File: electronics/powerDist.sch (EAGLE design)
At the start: 4 parts

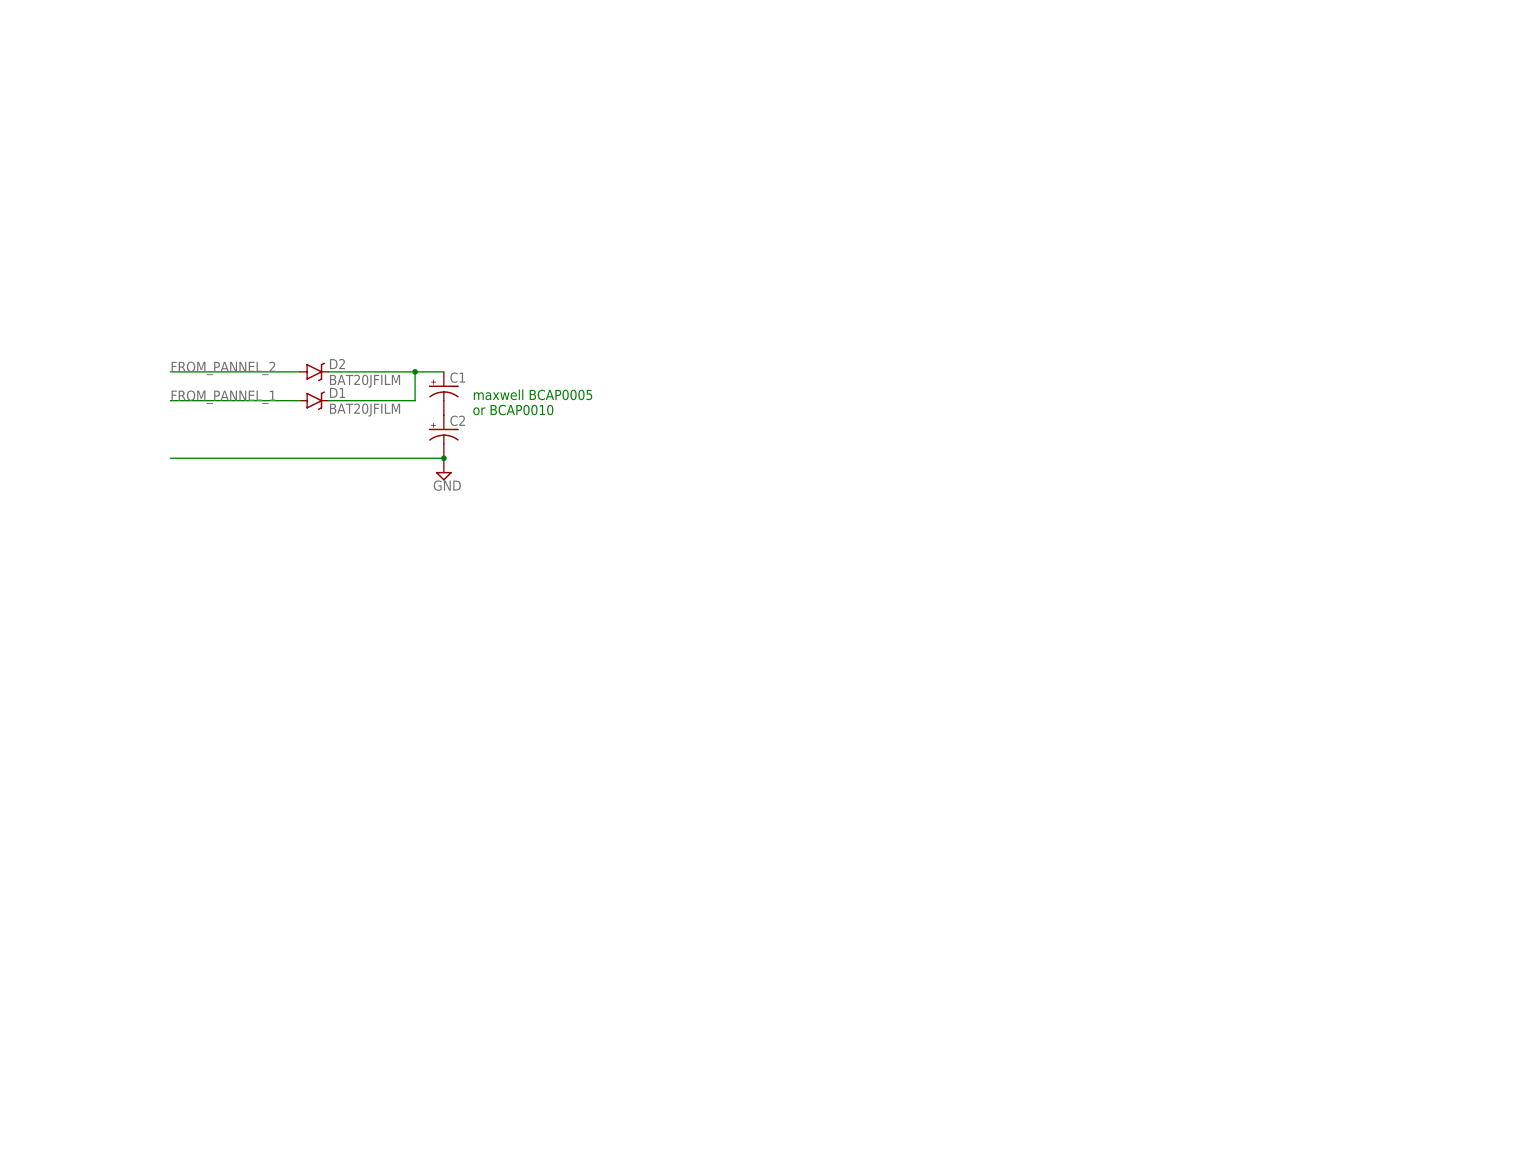
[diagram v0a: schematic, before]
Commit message: added msp430, went with drv ti motor drivers for galvos and brushed motor, max 1.8A
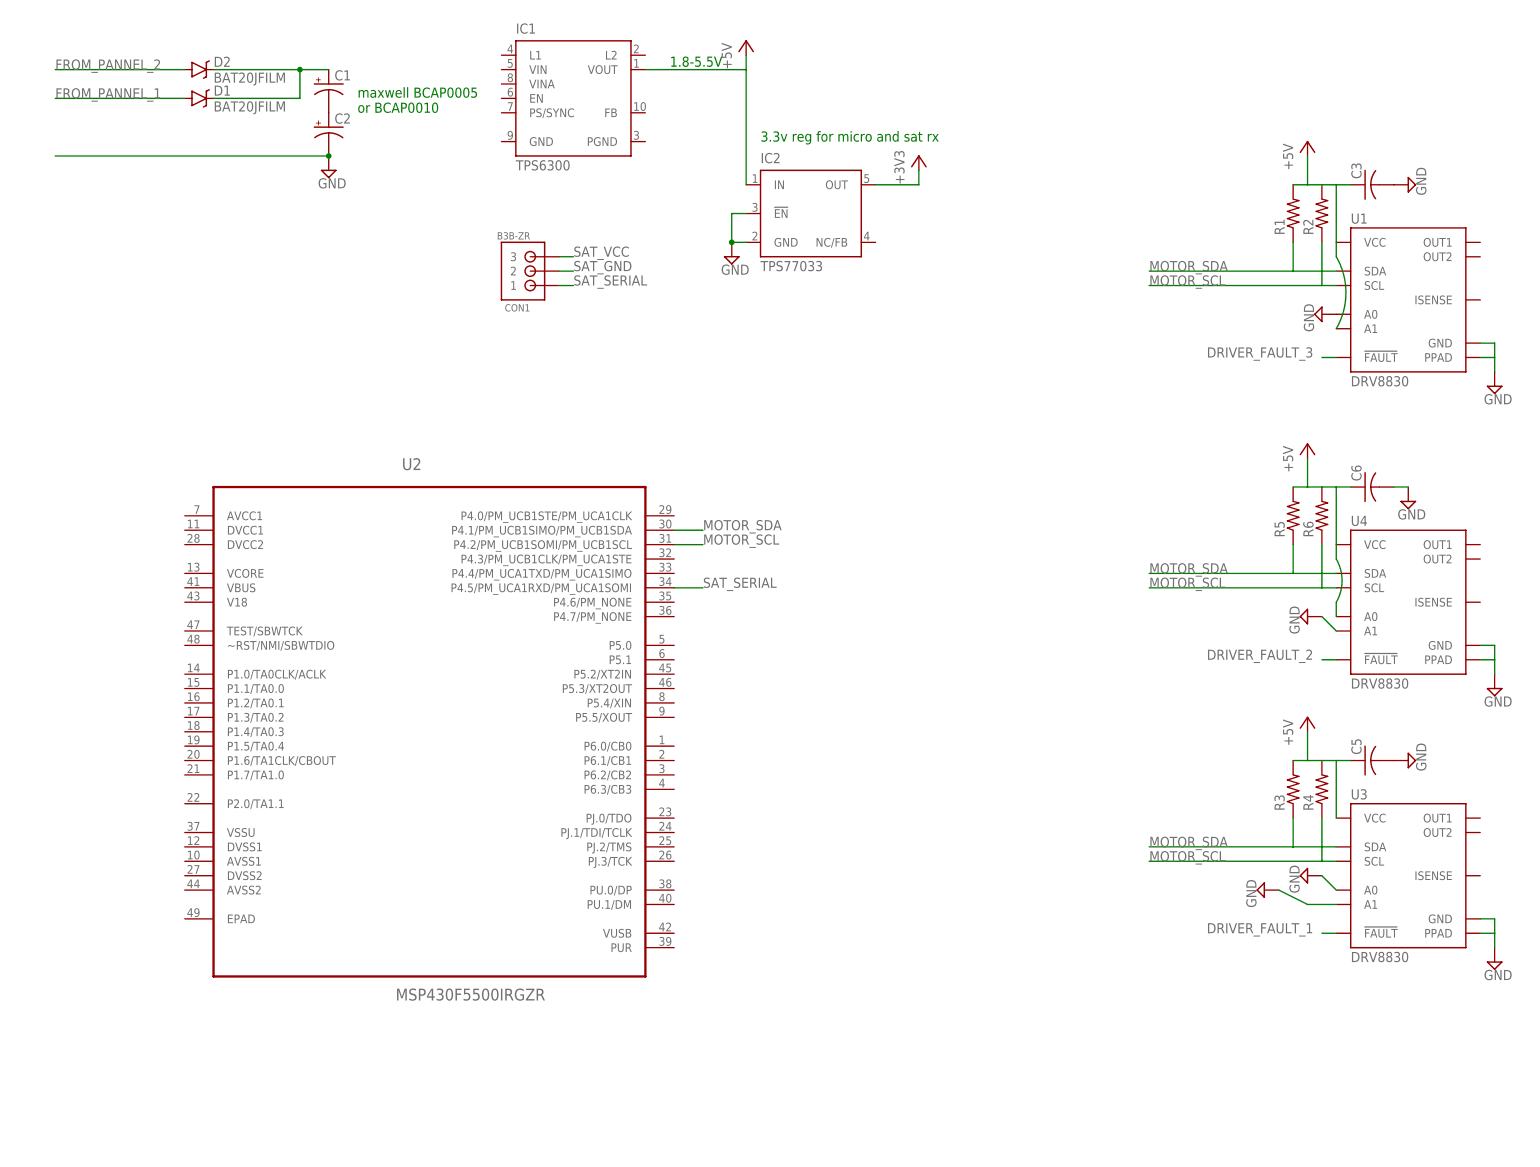
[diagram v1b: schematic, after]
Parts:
- added C3, C5, C6: (no value), rcl:C-USC0603
- added CON1: B3B-ZR, jst:B3B-ZR
- added IC1: TPS6300, texas:TPS6300
- added IC2: TPS77033, texas:TPS77033
- added R1, R2, R3, R4, R5, R6: (no value), rcl:R-US_R0402
- added U1, U3, U4: DRV8830, SparkFun-PowerIC:DRV8830
- added U2: MSP430F5500IRGZR, Texas Instruments_By_element14_Batch_1:MSP430F5500IRGZR
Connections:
- new net +3V3: IC2.OUT
- new net +5V: C3.1, C5.1, C6.1, IC1G$1.VOUT, IC2.IN, R1.2, R2.2, R3.2, R4.2, R5.2, R6.2, U1.A1, U1.VCC, U3.VCC, U4.A0, U4.VCC
- new net DRIVER_FAULT_1: U3.!FAULT
- new net DRIVER_FAULT_2: U4.!FAULT
- new net DRIVER_FAULT_3: U1.!FAULT
- new net MOTOR_SCL: R2.1, R4.1, R6.1, U1.SCL, U2.P4.2/PM_UCB1SOMI/PM_UCB1SCL, U3.SCL, U4.SCL
- new net MOTOR_SDA: R1.1, R3.1, R5.1, U1.SDA, U2.P4.1/PM_UCB1SIMO/PM_UCB1SDA, U3.SDA, U4.SDA
- new net SAT_GND: CON1.2
- new net SAT_SERIAL: CON1.1, U2.P4.5/PM_UCA1RXD/PM_UCA1SOMI
- new net SAT_VCC: CON1.3
- net GND: now also C3.2, C5.2, C6.2, IC2.!EN, IC2.GND, U1.A0, U1.GND, U1.PPAD, U3.A0, U3.A1, U3.GND, U3.PPAD, U4.A1, U4.GND, U4.PPAD
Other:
- note added: "1.8-5.5V"
- note added: "3.3v reg for micro and sat rx"
- moved on the sheet: C1, C2, D1, D2

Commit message: added passives to dc/dc.  todo figure out analog/micro stuff and connection points for motors
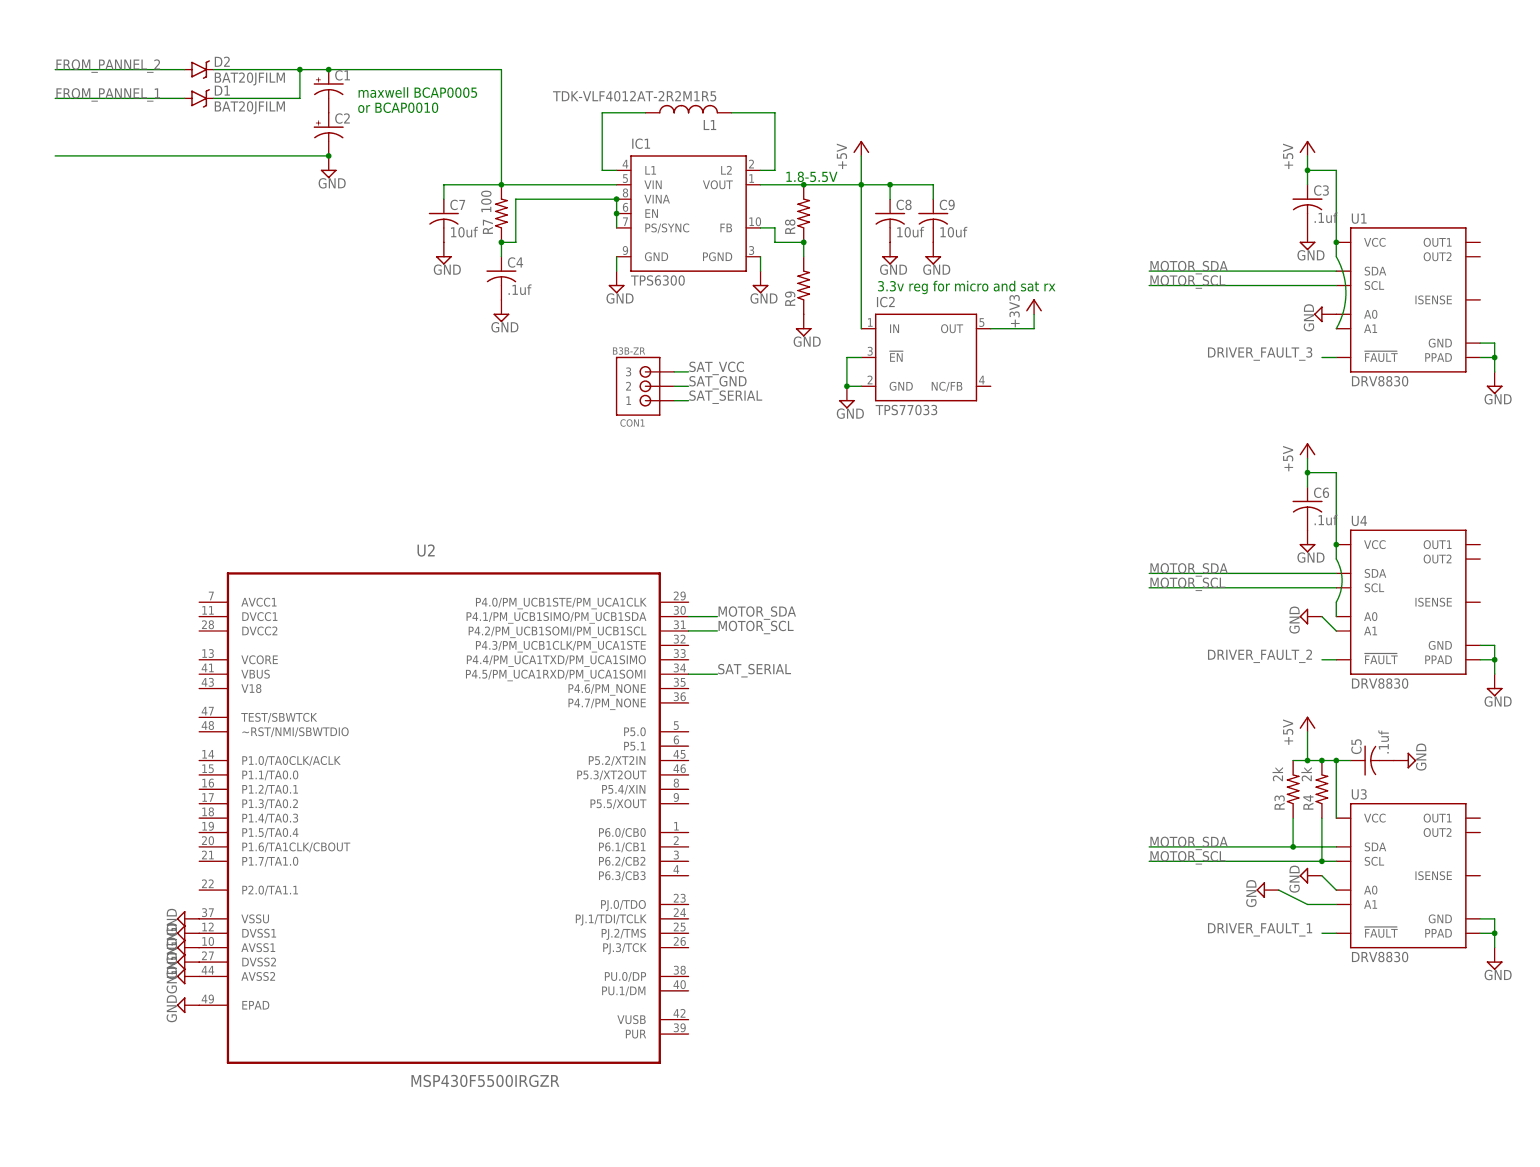
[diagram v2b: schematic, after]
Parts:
- removed R1, R2, R5, R6: (no value), rcl:R-US_R0402
- added C4: .1uf, rcl:C-USC0603
- added C7, C8, C9: 10uf, rcl:C-USC0603
- added L1: TDK-VLF4012AT-2R2M1R5, passives:TDK-VLF4012AT-2R2M1R5
- added R7: 100, rcl:R-US_R0402
- added R8, R9: (no value), rcl:R-US_R0402
- C3, C5, C6: value (none) -> .1uf
- R3, R4: value (none) -> 2k
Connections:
- new net N$3: IC1G$1.L1, L1.1
- new net N$4: IC1G$1.L2, L1.2
- new net N$8: C4.1, IC1G$1.EN, IC1G$1.PS/SYNC, IC1G$1.VINA, R7.1
- new net N$9: IC1G$1.FB, R8.1, R9.2
- net +5V: now also C8.1, C9.1, R8.2; no longer R1.2, R2.2, R5.2, R6.2
- net GND: now also C4.2, C7.2, C8.2, C9.2, IC1G$1.GND, IC1G$1.PGND, R9.1, U2.AVSS1, U2.AVSS2, U2.DVSS1, U2.DVSS2, U2.EPAD, U2.VSSU
- net MOTOR_SCL: no longer R2.1, R6.1
- net MOTOR_SDA: no longer R1.1, R5.1
- net N$2: now also C7.1, IC1G$1.VIN, R7.2
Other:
- moved on the sheet: C3, C6, CON1, IC1, IC2, U2

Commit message: added decoupling to mcu
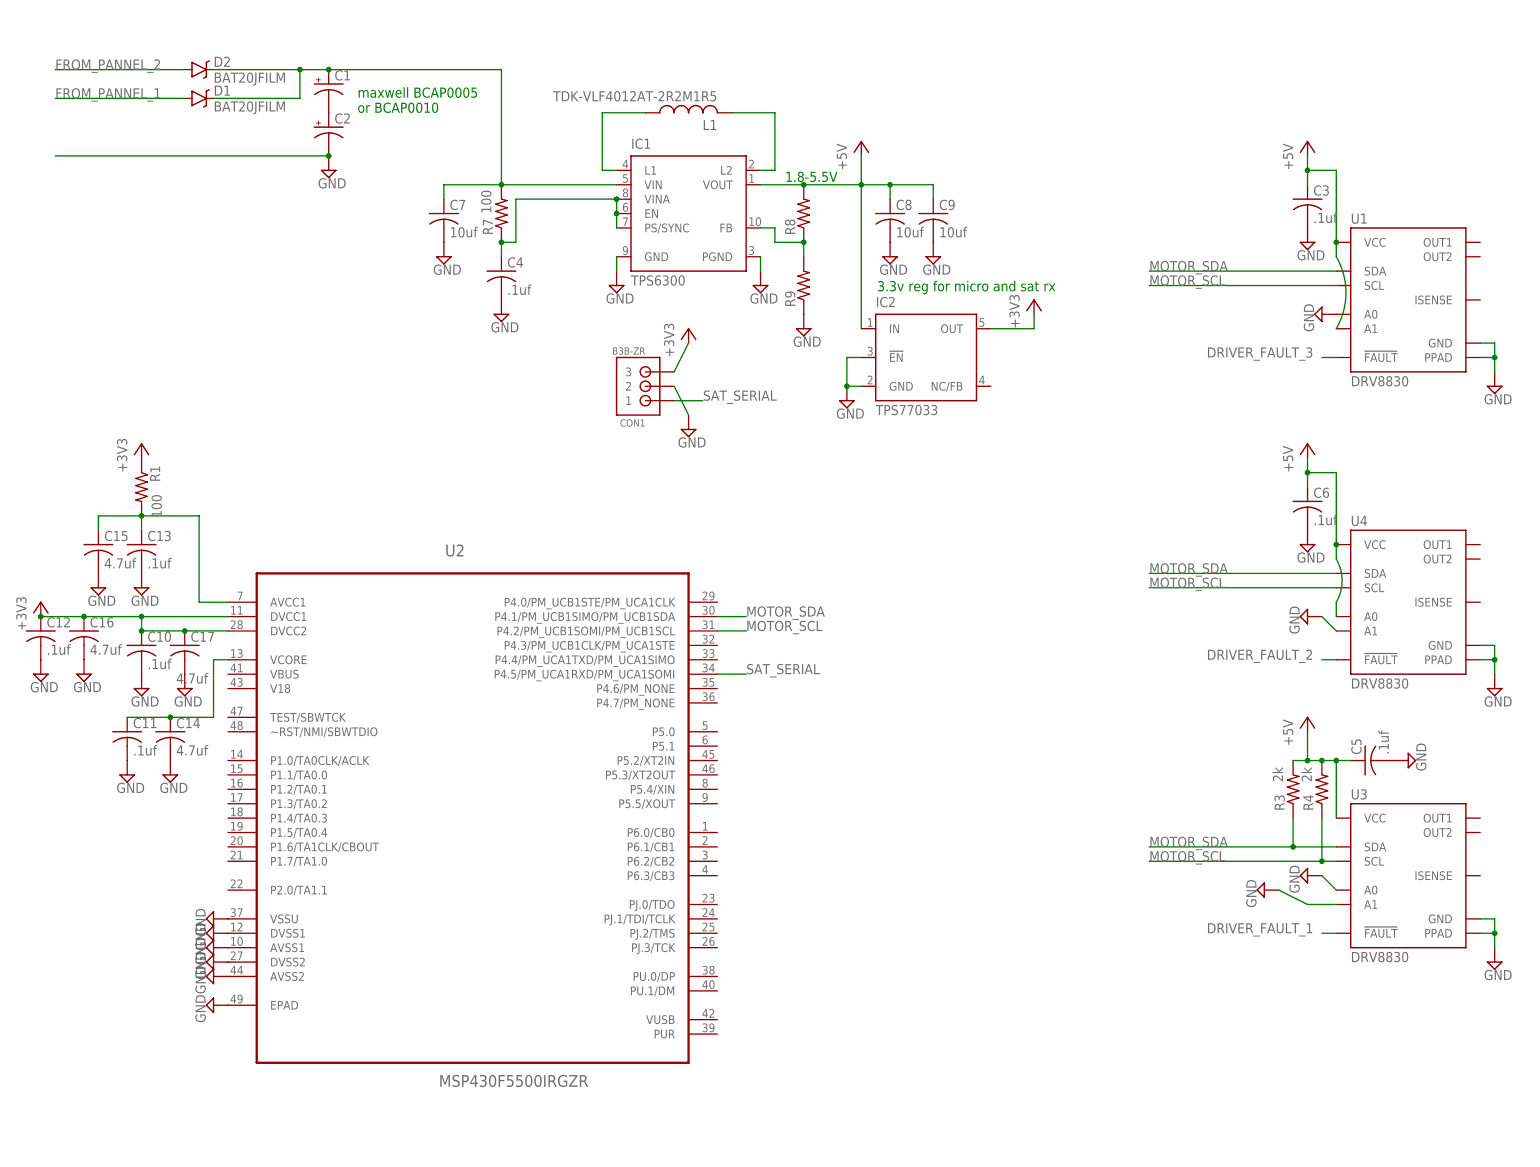
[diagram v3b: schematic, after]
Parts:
- added C10, C11, C12, C13: .1uf, rcl:C-USC0603
- added C14, C15, C16, C17: 4.7uf, rcl:C-USC0603
- added R1: 100, rcl:R-US_R0402
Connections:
- removed net SAT_GND: CON1.2
- removed net SAT_VCC: CON1.3
- new net N$5: C13.1, C15.1, R1.2, U2.AVCC1
- new net N$7: C11.1, C14.1, U2.VCORE
- net +3V3: now also C10.1, C12.1, C16.1, C17.1, CON1.3, R1.1, U2.DVCC1, U2.DVCC2
- net GND: now also C10.2, C11.2, C12.2, C13.2, C14.2, C15.2, C16.2, C17.2, CON1.2
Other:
- moved on the sheet: U2

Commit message: arraning components for layout.  May move to 402 passives if it gets too crowded.
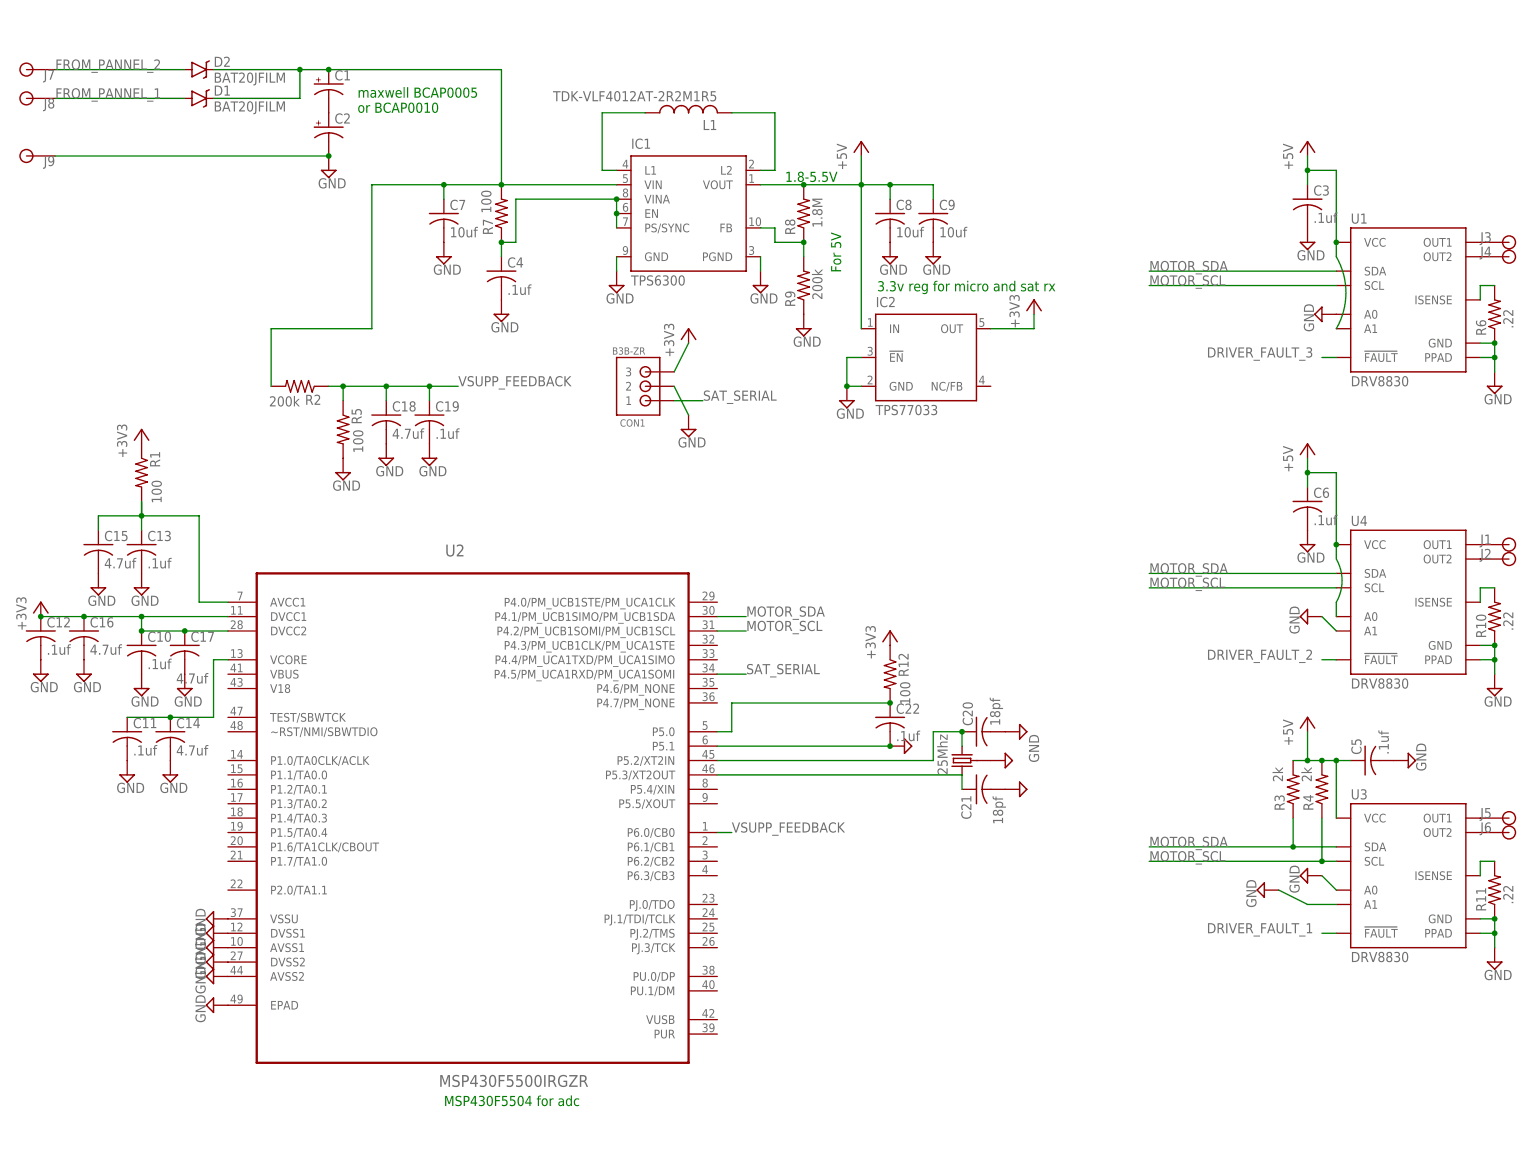
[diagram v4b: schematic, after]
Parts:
- added C18: 4.7uf, rcl:C-USC0603
- added C19, C22: .1uf, rcl:C-USC0603
- added C20, C21: 18pf, rcl:C-USC0603
- added J1, J2, J3, J4, J5, J6, J7, J8, J9: 2MMPAD, connectors:2MMPAD
- added R10, R11, R6: .22, rcl:R-US_R0402
- added R12, R5: 100, rcl:R-US_R0402
- added R2: 200k, rcl:R-US_R0402
- added U$1: 25Mhz, SparkFun-FreqCtrl:CRYSTAL-GROUNDED
- R8: value (none) -> 1.8M
- R9: value (none) -> 200k
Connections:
- new net N$10: J2.P$1, U4.OUT2
- new net N$11: J3.P$1, U1.OUT1
- new net N$12: J4.P$1, U1.OUT2
- new net N$13: J5.P$1, U3.OUT1
- new net N$14: J6.P$1, U3.OUT2
- new net N$15: C20.1, U$1.2, U2.P5.2/XT2IN
- new net N$16: C21.1, U$1.1, U2.P5.3/XT2OUT
- new net N$17: R6.2, U1.ISENSE
- new net N$18: R11.2, U3.ISENSE
- new net N$19: R10.2, U4.ISENSE
- new net N$20: C22.1, R12.2, U2.P5.0
- new net N$6: J1.P$1, U4.OUT1
- new net VSUPP_FEEDBACK: C18.1, C19.1, R2.1, R5.1, U2.P6.0/CB0
- net +3V3: now also R12.1
- net FROM_PANNEL_1: now also J8.P$1
- net FROM_PANNEL_2: now also J7.P$1
- net GND: now also C18.2, C19.2, C20.2, C21.2, C22.2, J9.P$1, R10.1, R11.1, R5.2, R6.1, U$1.3, U2.P5.1
- net N$2: now also R2.2
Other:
- note added: "For 5V"
- note added: "MSP430F5504 for adc"
- moved on the sheet: R1
